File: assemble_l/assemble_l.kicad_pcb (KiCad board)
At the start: 2 copper layers, 45 parts, among them J1 Conn_01x02_Pin, SW1 SW_Push, SW10 SW_Push, SW11 SW_Push, SW12 SW_Push, SW13 SW_Push, SW14 SW_Push, SW15 SW_Push, SW16 SW_Push, SW17 SW_Push, SW18 SW_Push, SW19 SW_Push, SW2 SW_Push, SW20 SW_Push, SW21 SW_Push, SW22 SW_Push, SW3 SW_Push, SW4 SW_Push, SW5 SW_Push, SW6 SW_Push, SW7 SW_Push, SW8 SW_Push, SW9 SW_Push, U1 Micon_BLEMicroPro

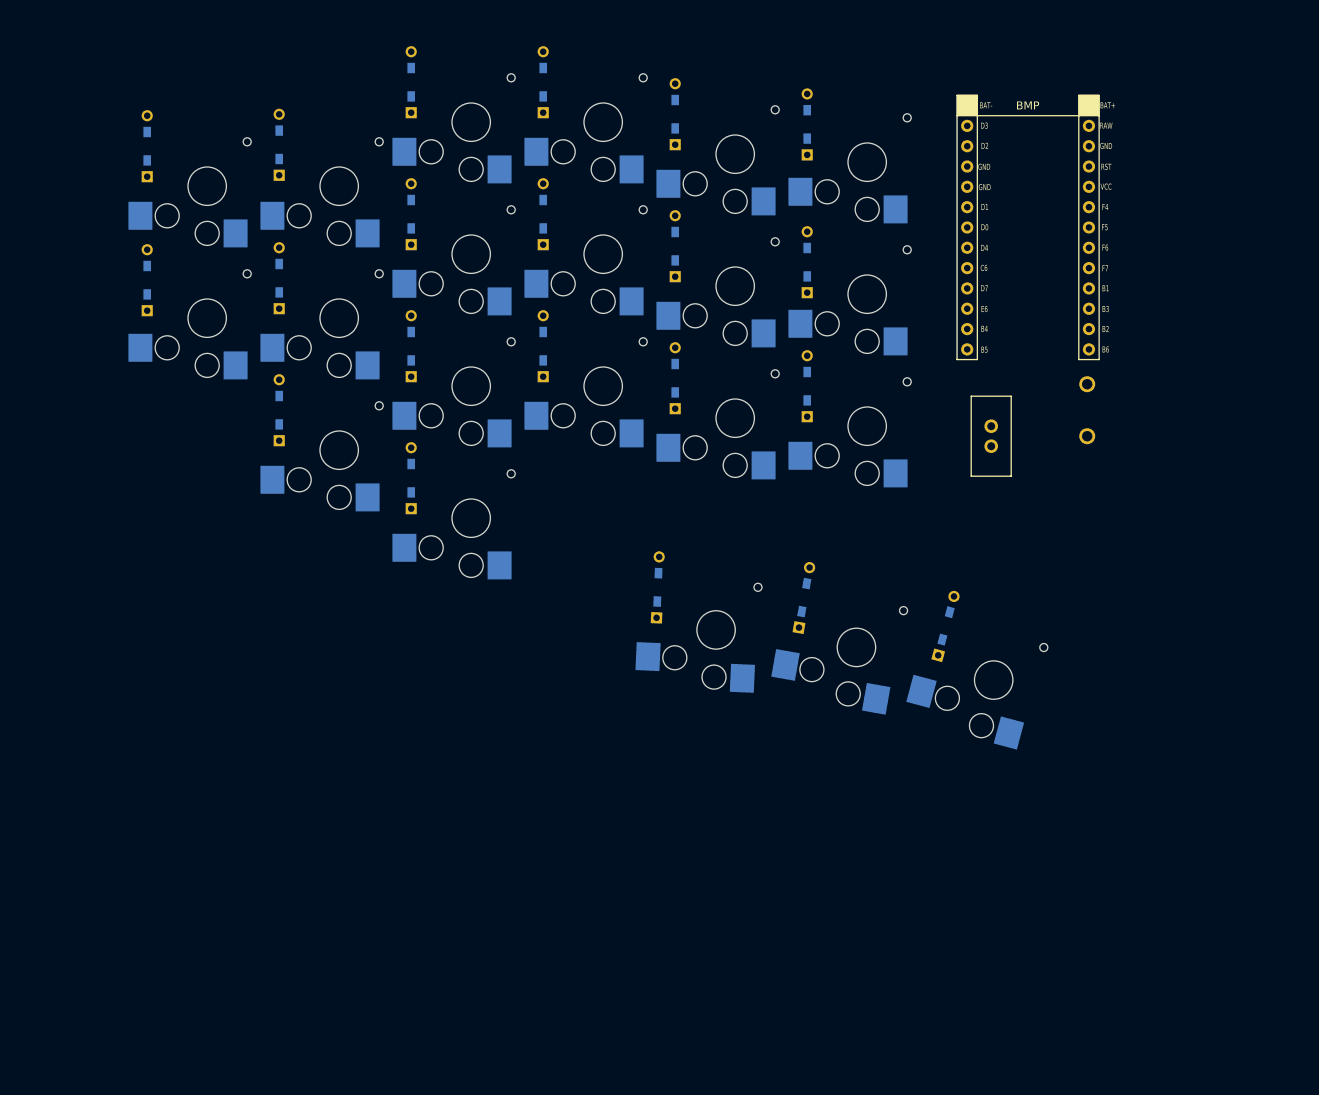
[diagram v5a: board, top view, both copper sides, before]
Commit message: fix: key layout
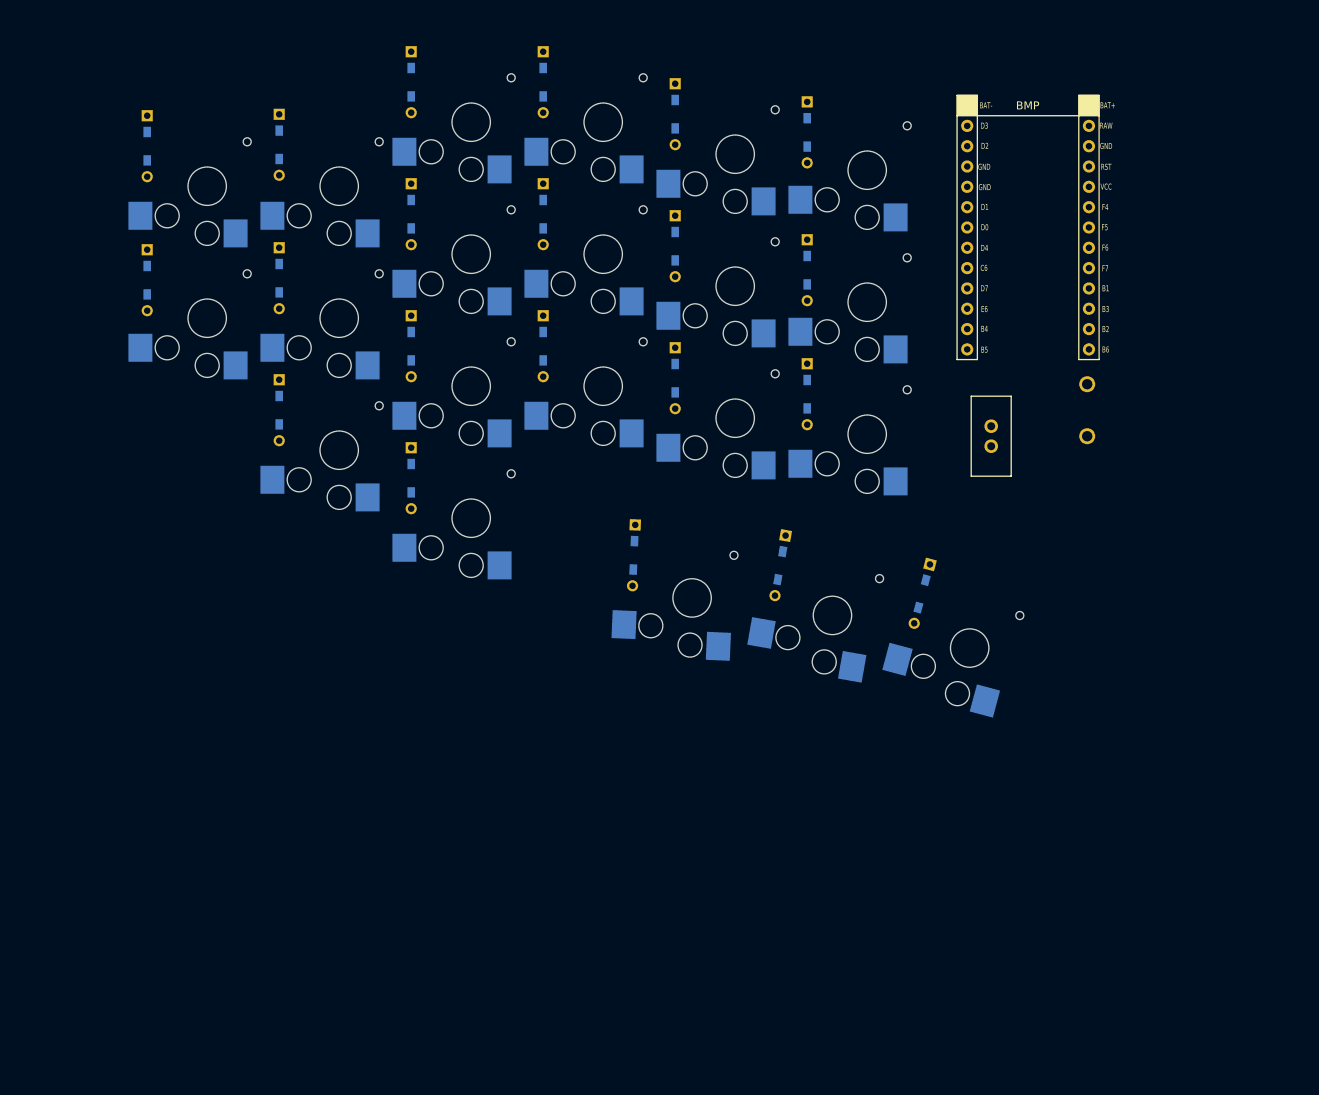
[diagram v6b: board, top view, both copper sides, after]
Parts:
- moved D13 5.00 mm to (121.3, 93.6), turned to -92.5 degrees
- moved D17 5.00 mm to (139.6, 94.9), turned to -100 degrees
- moved D21 5.00 mm to (157.4, 98.5), turned to -105 degrees
- moved SW13 5.00 mm to (128.6, 99.0)
- moved SW17 5.00 mm to (146.2, 101.2)
- moved SW21 5.00 mm to (163.3, 105.2)
- moved D18 1.00 mm to (143.0, 40.8), turned to -90 degrees
- moved D19 1.00 mm to (143.0, 58.0), turned to -90 degrees
- moved D20 1.00 mm to (143.0, 73.5), turned to -90 degrees
- moved SW18 1.00 mm to (150.5, 45.5)
- moved SW19 1.00 mm to (150.5, 62.0)
- moved SW20 1.00 mm to (150.5, 78.5)
- turned D1 to -90 degrees
- turned D10 to -90 degrees
- turned D11 to -90 degrees
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
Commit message: feat: add outline
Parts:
- moved D11 15.5 mm to (125.0, 55.0)
- moved D12 15.2 mm to (124.5, 72.0)
- moved D10 15.1 mm to (125.0, 36.0)
- moved D20 15.1 mm to (158.0, 75.0)
- moved D9 15.1 mm to (108.5, 85.5)
- moved D18 15.0 mm to (158.0, 42.0)
- moved D19 15.0 mm to (158.0, 58.5)
- moved D3 14.5 mm to (91.5, 43.5)
- moved D4 14.5 mm to (91.5, 59.5)
- moved D21 13.9 mm to (171.0, 101.0), turned to 75 degrees
- moved D6 9.01 mm to (94.0, 43.5)
- moved D8 9.00 mm to (93.5, 76.5)
- moved D16 8.51 mm to (127.0, 80.0)
- moved D7 8.51 mm to (94.0, 59.5)
- moved D1 8.50 mm to (60.5, 51.0)
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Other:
- board outline added: 128.5 x 92.1 mm

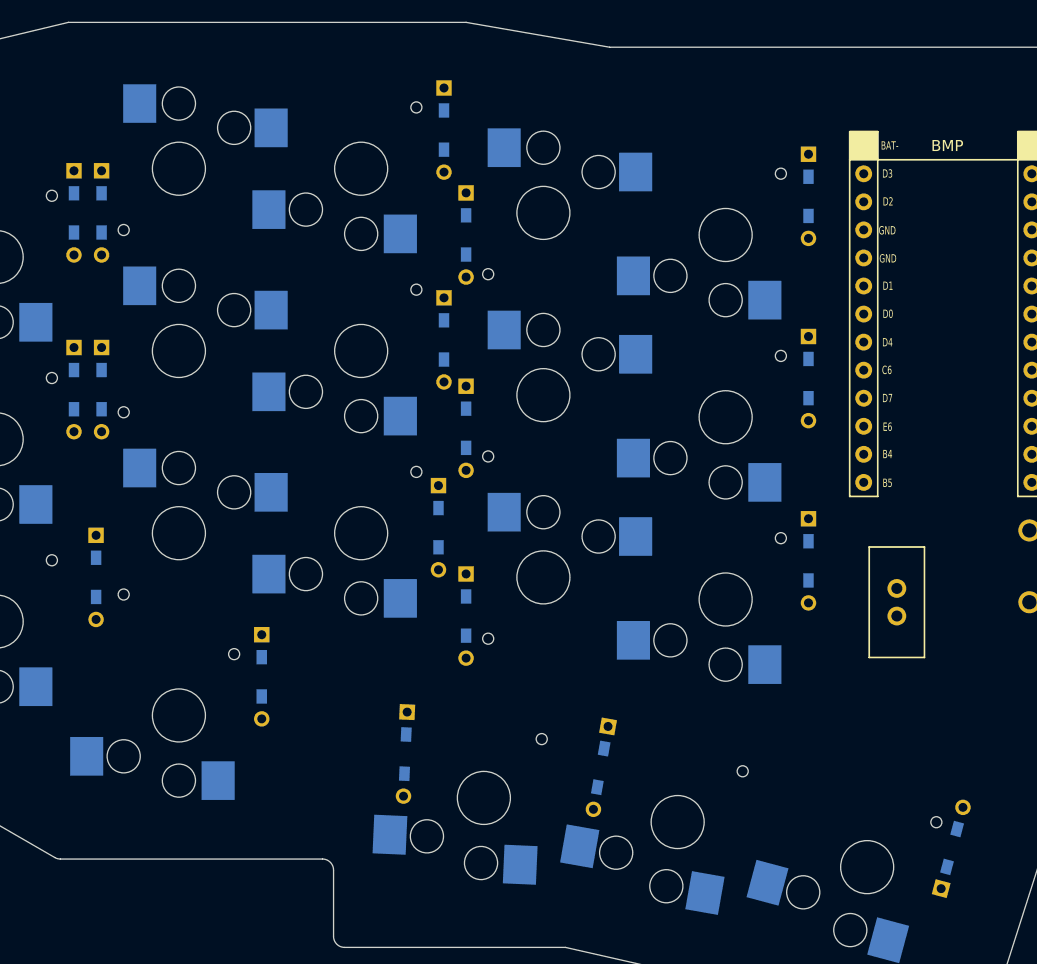
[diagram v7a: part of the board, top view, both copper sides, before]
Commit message: fix: place of diode
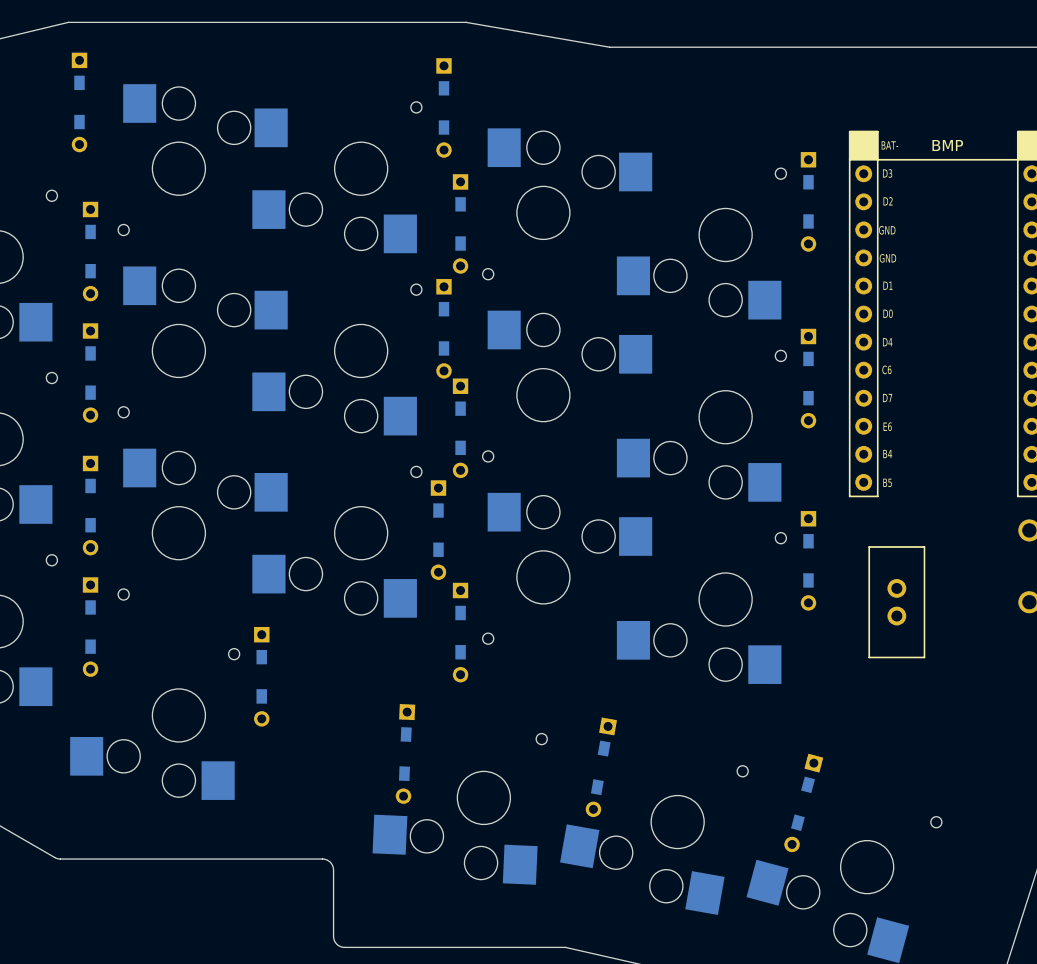
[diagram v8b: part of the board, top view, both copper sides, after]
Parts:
- moved D21 14.1 mm to (157.5, 97.0), turned to -105 degrees
- moved D4 10.6 mm to (93.0, 70.0)
- moved D6 10.2 mm to (92.0, 33.5)
- moved D8 4.53 mm to (93.0, 81.0)
- moved D3 3.81 mm to (93.0, 47.0)
- moved D10 2.00 mm to (125.0, 34.0)
- moved D7 1.80 mm to (93.0, 58.0)
- moved D16 1.58 mm to (126.5, 81.5)
- moved D14 1.12 mm to (126.5, 44.5)
- moved D11 1.00 mm to (125.0, 54.0)
- moved D15 0.50 mm to (126.5, 63.0)
- moved D18 0.50 mm to (158.0, 42.5)
- moved D12 0.22 mm to (124.5, 72.2)
